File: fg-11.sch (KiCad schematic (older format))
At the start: 75 parts, among them J1 Conn_02x05_Counter_Clockwise, J2 Conn_02x05_Counter_Clockwise, U1 ProMicro

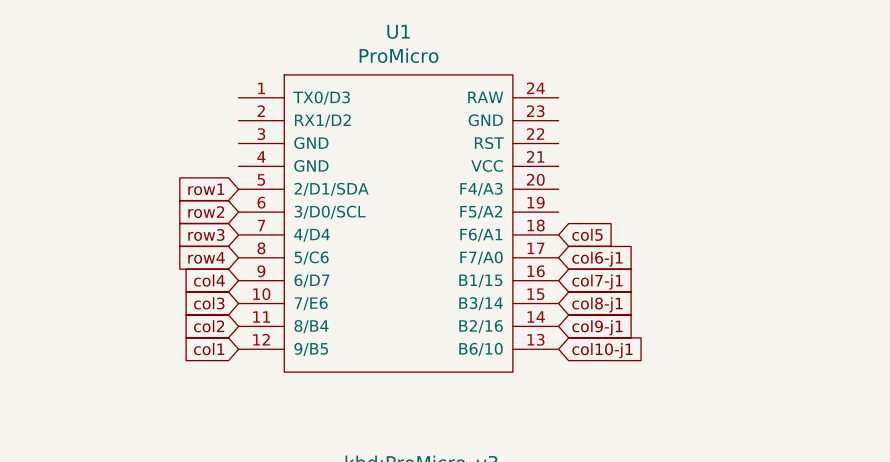
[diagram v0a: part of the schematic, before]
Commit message: First go at revision 2.
Revision 2 has several goals:

- Shift the index and ring finger one column outward, giving the
  index finger two columns each and the little fingers one each.
- Flip the controller. It was handy to have it the other way up for
  access to the reset button on an elite-c, but the on-board LED
  is bright blue and distracting.
- Add a reset button. By doing this any pro-micro footprint
  controller can now be used.
- Re-align the diodes. Many weren't quite aligned in rev-1 and it
  irked me.
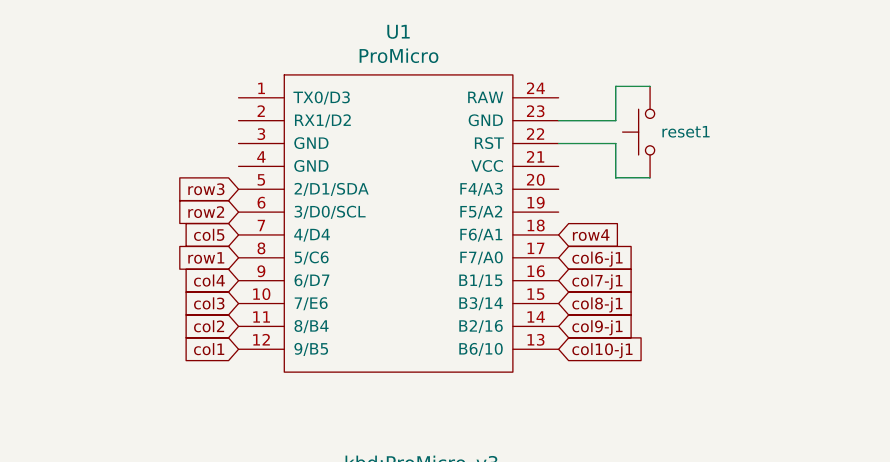
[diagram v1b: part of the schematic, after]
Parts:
- added reset1: SW_Push, kbd:ResetSW_1side, symbol Switch:SW_Push
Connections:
- net col5: now also U1.7 (4/D4); no longer U1.18 (F6/A1)
- net row1: now also U1.8 (5/C6); no longer U1.5 (2/D1/SDA)
- net row3: now also U1.5 (2/D1/SDA); no longer U1.7 (4/D4)
- net row4: now also U1.18 (F6/A1); no longer U1.8 (5/C6)
- net at U1.22 (RST): now also reset1.1
- net at U1.23 (GND): now also reset1.2
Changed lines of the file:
@@
 Text GLabel 5800 5750 2    50   Input ~ 0
 col6-j2
-Text GLabel 5050 1600 0    50   Input ~ 0
+Text GLabel 5050 1900 0    50   Input ~ 0
 row1
 Text GLabel 5050 1700 0    50   Input ~ 0
 row2
-Text GLabel 5050 1800 0    50   Input ~ 0
+Text GLabel 5050 1600 0    50   Input ~ 0
 row3
-Text GLabel 5050 1900 0    50   Input ~ 0
+Text GLabel 6450 1800 2    50   Input ~ 0
 row4
 Text GLabel 5050 2300 0    50   Input ~ 0
@@
 Text GLabel 5050 2000 0    50   Input ~ 0
 col4
-Text GLabel 6450 1800 2    50   Input ~ 0
+Text GLabel 5050 1800 0    50   Input ~ 0
 col5
 Text GLabel 6450 1900 2    50   Input ~ 0
@@
 	7950 5300 7950 6000
 Connection ~ 7950 5300
+$Comp
+L Switch:SW_Push reset1
+U 1 1 635F7836
+P 6850 1350
+F 0 "reset1" V 6850 1302 50  0000 R CNN
+F 1 "SW_Push" V 6805 1302 50  0001 R CNN
+F 2 "kbd:ResetSW_1side" H 6850 1550 50  0001 C CNN
+F 3 "~" H 6850 1550 50  0001 C CNN
+	1    6850 1350
+	0    -1   -1   0
+$EndComp
+Wire Wire Line
+	6850 1550 6700 1550
+Wire Wire Line
+	6700 1550 6700 1400
+Wire Wire Line
+	6700 1400 6450 1400
+Wire Wire Line
+	6850 1150 6700 1150
+Wire Wire Line
+	6700 1150 6700 1300
+Wire Wire Line
+	6700 1300 6450 1300
 $EndSCHEMATC
